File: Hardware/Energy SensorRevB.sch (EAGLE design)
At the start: 42 parts, among them IC1 7805, IC2 ATMega328p-pu, IC3 ld33v, Q1 16MHz, X1 MAINS IN, X2 MAINS OUT

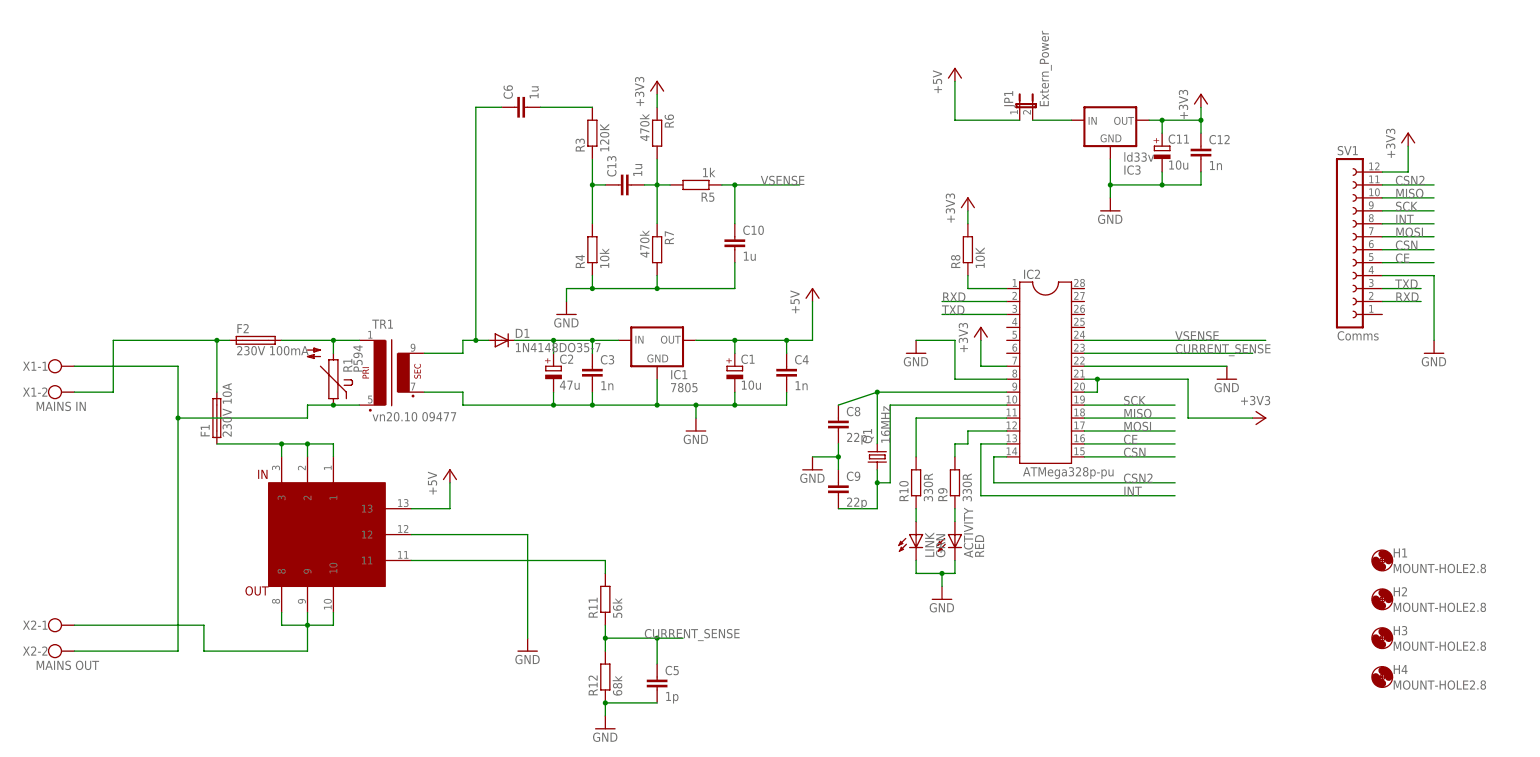
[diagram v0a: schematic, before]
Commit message: updated scematic with new power regulator and 3.5mm jack connector for current meter
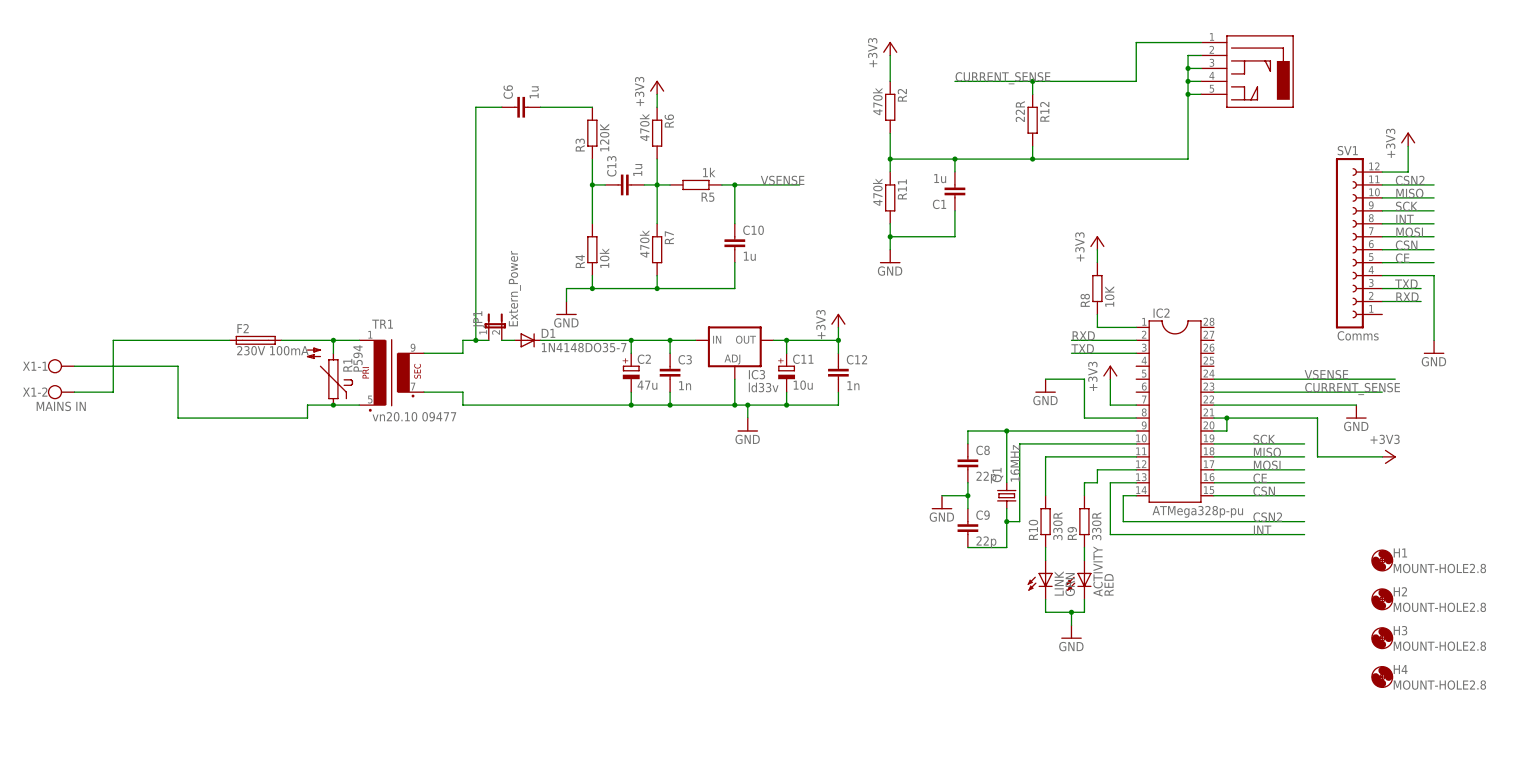
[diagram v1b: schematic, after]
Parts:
- removed C4: 1n, rcl:C-EU025-025X050
- removed C5: 1p, rcl:C-EU025-025X050
- removed F1: 230V 10A, fuse:SH22,5A
- removed IC1: 7805, v-reg:78XXL
- removed X2: MAINS OUT, con-wago-500:W237-102
- added R2: 470k, rcl:R-EU_0207/7
- C1: value 10u -> 1u; device rcl:CPOL-EUE2.5-6 -> rcl:C-EU025-025X050
- IC3: device v-reg:79XXL -> v-reg:LM317TL
- R11: value 56k -> 470k
- R12: value 68k -> 22R
- U$1: value CAS25-NP -> 3.5MMJACK; device CAS:CAS25-NP -> jack:3.5MMJACK
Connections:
- removed net +5V: C1.+, C4.1, IC1.OUT, JP1.1, U$1.13
- removed net N$11: R11.2, U$1.11
- removed net N$6: F1.1, U$1.1, U$1.2, U$1.3
- removed net N$8: U$1.10, U$1.8, U$1.9, X2-1.KL
- new net N$1: C1.2, R11.1, R12.2, R2.2, U$1.P$2, U$1.P$3, U$1.P$4, U$1.P$5
- net +3V3: now also R2.1
- net CURRENT_SENSE: now also R12.1, U$1.P$1; no longer C5.1, R11.1, R12.2
- net GND: now also C1.1, IC3.ADJ, R11.2; no longer C1.-, C4.2, C5.2, IC1.GND, IC3.GND, R12.1, U$1.12
- net N$2: no longer X2-2.KL
- net N$22: no longer F1.2
- net N$3: now also D1.A; no longer IC3.IN
- net N$5: now also JP1.1; no longer D1.A
- net N$7: now also IC3.IN; no longer IC1.IN
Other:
- moved on the sheet: ACTIVITY, C11, C12, C2, C3, C8, C9, D1, IC2, IC3, JP1, LINK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

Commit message: Updated Rev B to reflect beneficial changes with Rev A pratical application, added noise suppressor to ARef. updated smoothing Ref Caps to match package. Added Additional Smoothing capacitors (due to unsteady supply) removed 5V Regulator. updated to new CT. Moved to smaller footprint. corrected Smoothing cap connected at incorrect place
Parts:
- added C4: 10u, rcl:CPOL-EUE3.5-8
- added C5: 100n, rcl:C-EUC1206K
- added L1: (no value), rcl:L-EUL3230M
- added R13: 1k, rcl:R-EU_0207/7
- C1, C10: value 1u -> 10u; device rcl:C-EU025-025X050 -> rcl:C-EUC1206K
- C11: device rcl:CPOL-EUE2.5-6 -> rcl:CPOL-EUE3.5-8
- C13, C6: device rcl:C-EU025-025X050 -> rcl:C-EUC1206K
- C2: device rcl:CPOL-EUE2.5-6 -> rcl:CPOL-EUE3.5-10
- R12: device rcl:R-EU_0207/7 -> rcl:R-EU_R1206
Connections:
- new net N$6: R12.1, R13.1, U$1.P$1
- new net N$8: C5.1, IC2.21, L1.1
- net +3V3: now also C4.+, L1.2; no longer IC2.21
- net CURRENT_SENSE: now also R13.2; no longer R12.1, U$1.P$1
- net GND: now also C4.-, C5.2
- net N$10: now also C10.1
- net VSENSE: no longer C10.1
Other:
- moved on the sheet: R5

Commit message: general tidying up before manufacture
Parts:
- L1: value (none) -> 10u
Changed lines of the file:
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@@
 <part name="C4" library="rcl" deviceset="CPOL-EU" device="E3.5-8" value="10u"/>
 <part name="C5" library="rcl" deviceset="C-EU" device="C1206K" value="100n"/>
-<part name="L1" library="rcl" deviceset="L-EU" device="L3230M"/>
+<part name="L1" library="rcl" deviceset="L-EU" device="L3230M" value="10u"/>
 </parts>
 <sheets>
